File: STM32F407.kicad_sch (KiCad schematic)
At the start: 26 parts, among them J901 UART_CONN, J902 CAN_CONN, SW901 SW_SPDT, U901 STM32F407VGTx, Y901 8MHz

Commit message: layout re-design start
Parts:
- Y901: footprint Crystal:Crystal_SMD_0603-2Pin_6.0x3.5mm_HandSoldering -> Crystal:Crystal_SMD_0603-2Pin_6.0x3.5mm
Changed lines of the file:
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@@
 			)
 		)
-		(property "Footprint" "Crystal:Crystal_SMD_0603-2Pin_6.0x3.5mm_HandSoldering"
+		(property "Footprint" "Crystal:Crystal_SMD_0603-2Pin_6.0x3.5mm"
 			(at 57.044 54.1273 0)
 			(effects

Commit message: ethernet, debugger and usb layouts re-designed
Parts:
- SW901: footprint Button_Switch_SMD:SW_Tactile_SPST_NO_Straight_CK_PTS636Sx25SMTRLFS -> Button_Switch_SMD:SW_SPST_B3U-1000P
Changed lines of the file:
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@@
 			)
 		)
-		(property "Footprint" "Button_Switch_SMD:SW_Tactile_SPST_NO_Straight_CK_PTS636Sx25SMTRLFS"
+		(property "Footprint" "Button_Switch_SMD:SW_SPST_B3U-1000P"
 			(at 30.742 85.6128 0)
 			(effects

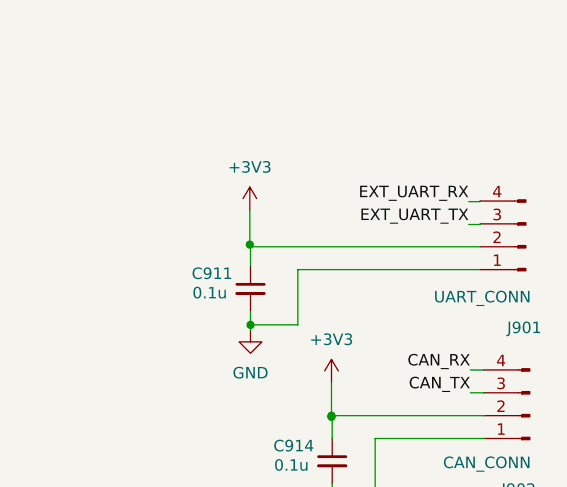
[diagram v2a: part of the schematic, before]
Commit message: MIC footprint changed, all blocks routed internally, next step is route all to the MCU
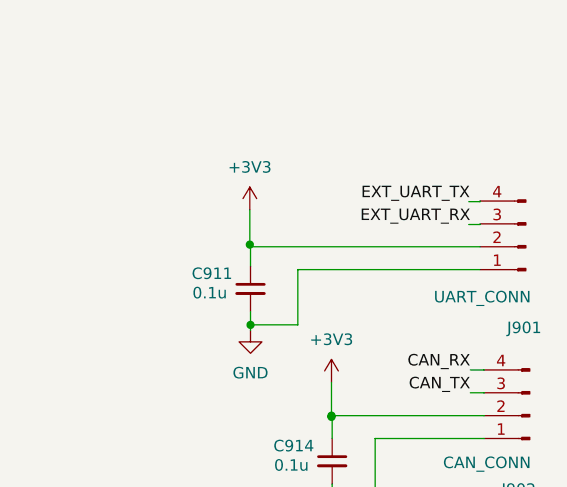
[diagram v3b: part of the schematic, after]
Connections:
- net EXT_UART_RX: now also J901.3 (Pin_3); no longer J901.4 (Pin_4)
- net EXT_UART_TX: now also J901.4 (Pin_4); no longer J901.3 (Pin_3)
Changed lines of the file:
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@@
 	)
 	(label "EXT_UART_RX"
-		(at 266.7 31.75 180)
+		(at 266.8813 34.29 180)
 		(fields_autoplaced yes)
 		(effects
@@
 	)
 	(label "EXT_UART_TX"
-		(at 266.7 34.29 180)
+		(at 266.8284 31.75 180)
 		(fields_autoplaced yes)
 		(effects

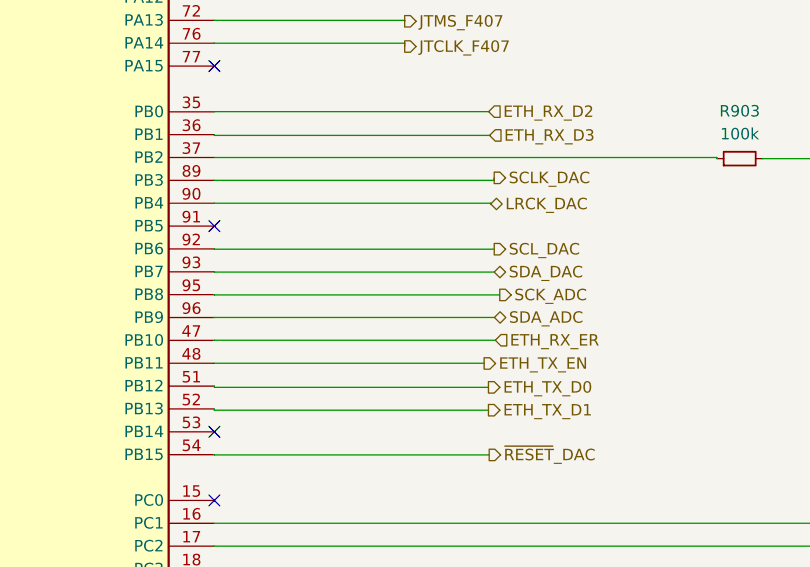
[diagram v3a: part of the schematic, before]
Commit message: some design failures reviewed(MIC VDD is 1V8, Motor Drivers' pull-up to DVDD pin, I2C net fixed). Routing mostly done.
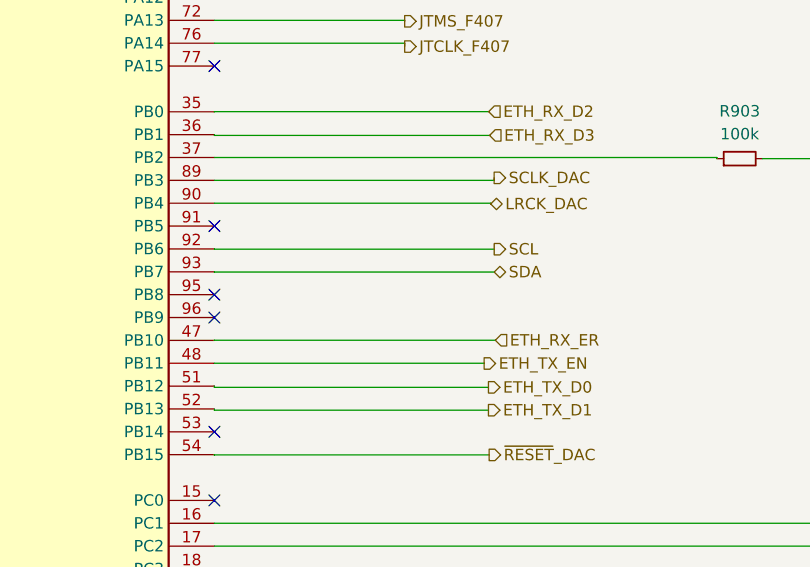
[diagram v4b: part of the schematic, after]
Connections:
- net SCK_ADC: no longer names the net of U901.95 (PB8)
- net SCL_DAC renamed SCL
- net SDA_ADC: no longer names the net of U901.96 (PB9)
- net SDA_DAC renamed SDA
- no-connect marks 28 -> 30
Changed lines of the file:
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@@
+	)
+	(no_connect
+		(at 156.7969 101.6659)
 	)
 	(no_connect
@@
 	)
 	(no_connect
+		(at 156.7969 104.2059)
+	)
+	(no_connect
 		(at 111.0769 71.1859)
 	)
@@
 	(wire
 		(pts
-			(xy 187.9109 104.1987) (xy 156.7969 104.1987)
-		)
-		(stroke
-			(width 0)
-			(type default)
-		)
-	)
-	(wire
-		(pts
 			(xy 35.719 83.6951) (xy 35.719 85.5894)
 		)
@@
 		(pts
 			(xy 91.2355 22.7055) (xy 83.6821 22.7055)
-		)
-		(stroke
-			(width 0)
-			(type default)
-		)
-	)
-	(wire
-		(pts
-			(xy 188.5035 101.6966) (xy 156.7969 101.6966)
 		)
 		(stroke
@@
 		)
 	)
-	(hierarchical_label "SDA_ADC"
-		(shape bidirectional)
-		(at 187.9109 104.1987 0)
-		(fields_autoplaced yes)
-		(effects
-			(font
-				(size 1.27 1.27)
-			)
-			(justify left)
-		)
-	)
 	(hierarchical_label "ETH_MDC"
 		(shape output)
@@
 		)
 	)
-	(hierarchical_label "SCL_DAC"
+	(hierarchical_label "SCL"
 		(shape output)
 		(at 187.8893 96.6121 0)
@@
 		)
 	)
-	(hierarchical_label "SCK_ADC"
-		(shape output)
-		(at 188.5035 101.6966 0)
-		(fields_autoplaced yes)
-		(effects
-			(font
-				(size 1.27 1.27)
-			)
-			(justify left)
-		)
-	)
 	(hierarchical_label "ETH_RX_ER"
 		(shape input)
@@
 		)
 	)
-	(hierarchical_label "SDA_DAC"
+	(hierarchical_label "SDA"
 		(shape bidirectional)
 		(at 187.8893 99.1521 0)

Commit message: some additions
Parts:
- renumbered C908 to C?, C909 to C?, C911 to C?, C902 to C?, C916 to C?, C913 to C?, C912 to C?, C910 to C?, C905 to C?, C915 to C?, C917 to C?, C914 to C?, C901 to C?, C903 to C?, C904 to C?, C906 to C?, C907 to C?, FB901 to FB?, J902 to J?, J901 to J?, R902 to R?, R903 to R?, R901 to R?, SW901 to SW?, U901 to U?, Y901 to Y?
